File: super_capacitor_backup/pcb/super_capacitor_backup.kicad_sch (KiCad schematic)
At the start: 24 parts, among them J1 Vin, J2 GND, J3 Vout, J4 GND, Q1 PMBT3906.235, Q2 DMP4065S-7, Q3 PMBT3906.235, Q4 PMBT3906.235, Q5 PMBT3906.235, Q6 PMBT3906.235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

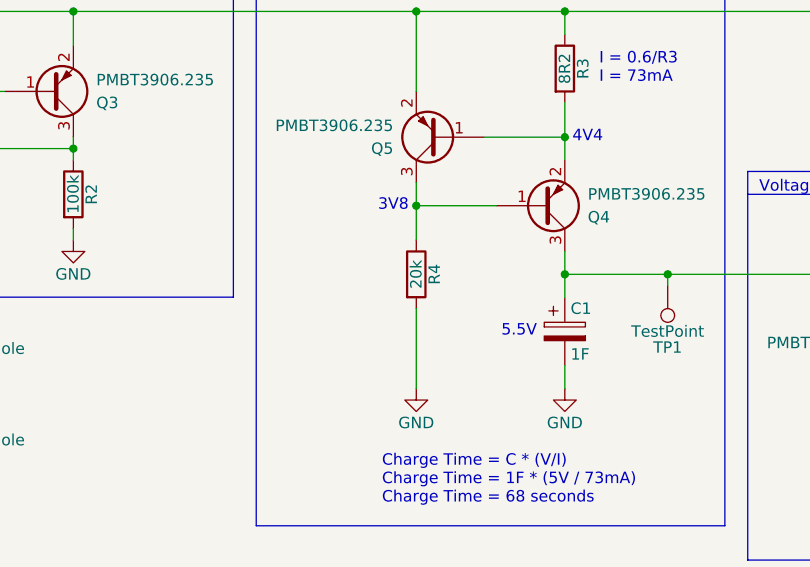
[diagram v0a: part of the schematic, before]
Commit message: increase bias current
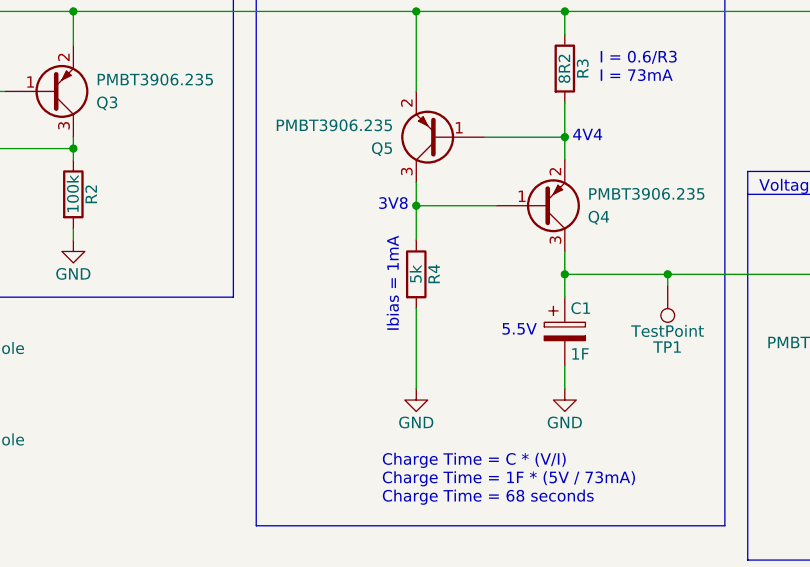
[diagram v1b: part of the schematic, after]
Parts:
- R4: value 20k -> 5k
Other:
- note added: "Ibias = 1mA"
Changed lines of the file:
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@@
+		)
+	)
+	(text "Ibias = 1mA"
+		(exclude_from_sim no)
+		(at 132.08 85.09 90)
+		(effects
+			(font
+				(size 1.27 1.27)
+			)
 		)
 	)
@@
 			)
 		)
-		(property "Value" "20k"
+		(property "Value" "5k"
 			(at 134.62 83.82 90)
 			(effects
